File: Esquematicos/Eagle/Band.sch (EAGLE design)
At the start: 11 parts

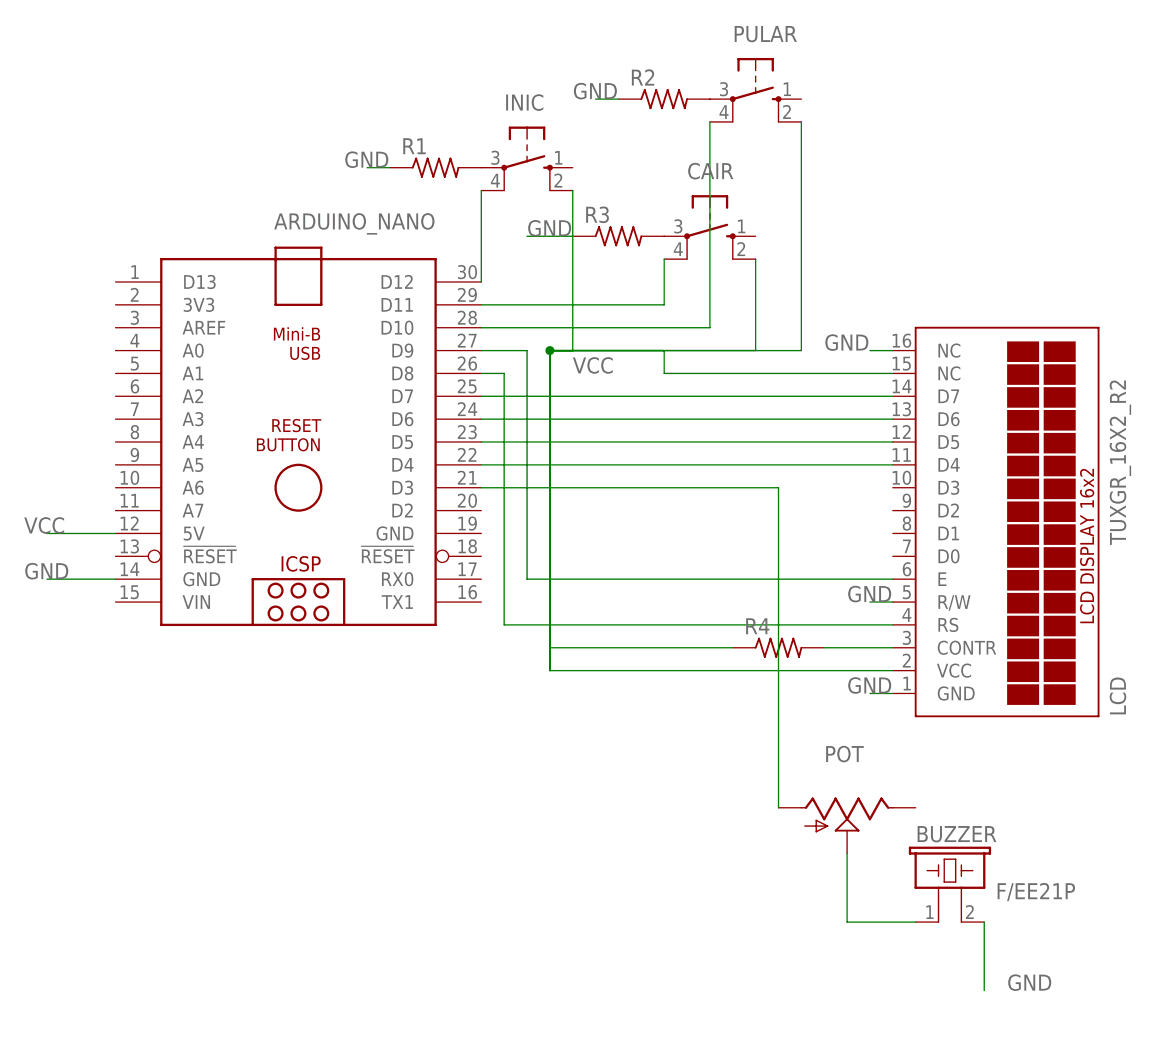
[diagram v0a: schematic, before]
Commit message: Editando Esquemático Eagle Band
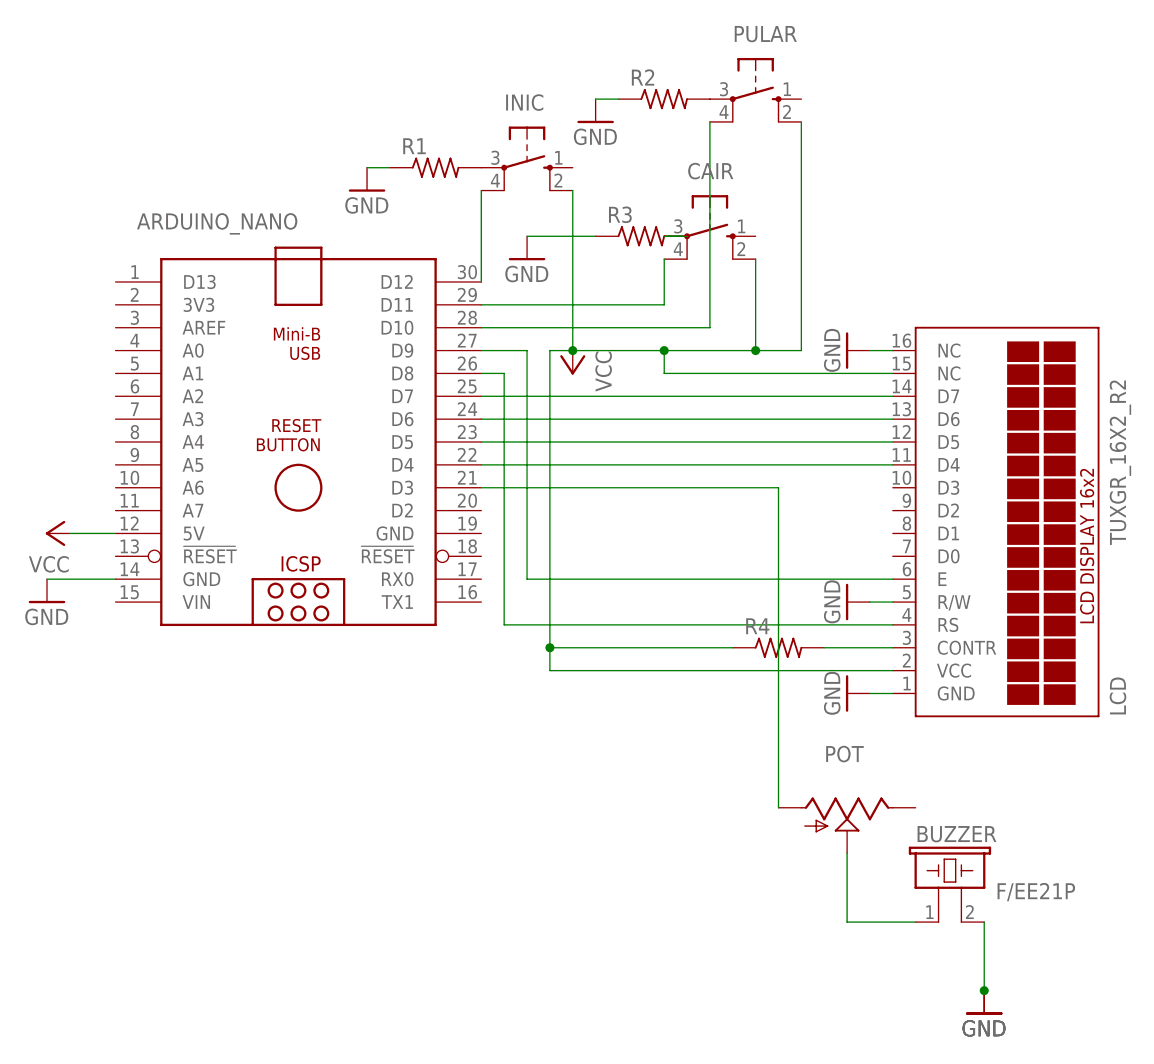
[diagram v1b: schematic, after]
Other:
- moved on the sheet: R3

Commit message: PCB da Band add
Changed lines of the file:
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@@
 <?xml version="1.0" encoding="utf-8"?>
 <!DOCTYPE eagle SYSTEM "eagle.dtd">
-<eagle version="9.6.1">
+<eagle version="9.1.0">
 <drawing>
 <settings>
-<setting alwaysvectorfont="no"/>
+<setting alwaysvectorfont="yes"/>
 <setting verticaltext="up"/>
 </settings>
@@
 <part name="GND7" library="supply1" library_urn="urn:adsk.eagle:library:371" deviceset="GND" device=""/>
 <part name="GND8" library="supply1" library_urn="urn:adsk.eagle:library:371" deviceset="GND" device=""/>
-<part name="GND9" library="supply1" library_urn="urn:adsk.eagle:library:371" deviceset="GND" device=""/>
 <part name="GND10" library="supply1" library_urn="urn:adsk.eagle:library:371" deviceset="GND" device=""/>
 <part name="P+1" library="supply1" library_urn="urn:adsk.eagle:library:371" deviceset="VCC" device=""/>
@@
 <attribute name="VALUE" x="114.3" y="144.78" size="1.778" layer="96"/>
 </instance>
-<instance part="GND9" gate="1" x="160.02" y="48.26" smashed="yes">
-<attribute name="VALUE" x="157.48" y="45.72" size="1.778" layer="96"/>
-</instance>
-<instance part="GND10" gate="1" x="160.02" y="48.26" smashed="yes">
-<attribute name="VALUE" x="157.48" y="45.72" size="1.778" layer="96"/>
+<instance part="GND10" gate="1" x="160.02" y="50.8" smashed="yes">
+<attribute name="VALUE" x="157.48" y="48.26" size="1.778" layer="96"/>
 </instance>
 <instance part="P+1" gate="VCC" x="55.88" y="101.6" smashed="yes" rot="R90">
@@
 <segment>
 <pinref part="BUZZER" gate="G$1" pin="2"/>
-<wire x1="160.02" y1="58.42" x2="160.02" y2="50.8" width="0.1524" layer="91"/>
-<pinref part="GND9" gate="1" pin="GND"/>
+<wire x1="160.02" y1="58.42" x2="160.02" y2="53.34" width="0.1524" layer="91"/>
 <pinref part="GND10" gate="1" pin="GND"/>
-<junction x="160.02" y="50.8"/>
-</segment>
-<segment>
+</segment>
+<segment>

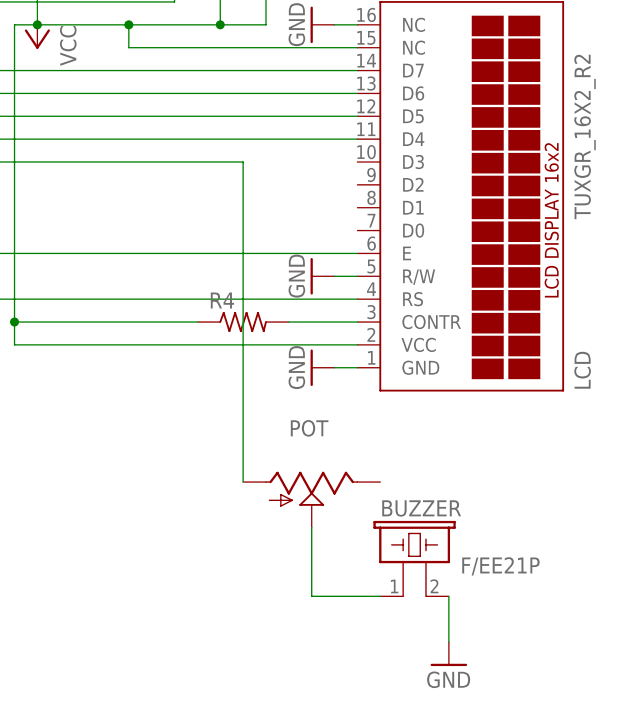
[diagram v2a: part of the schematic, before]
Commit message: Esquemático atualizado com os componentes 3D
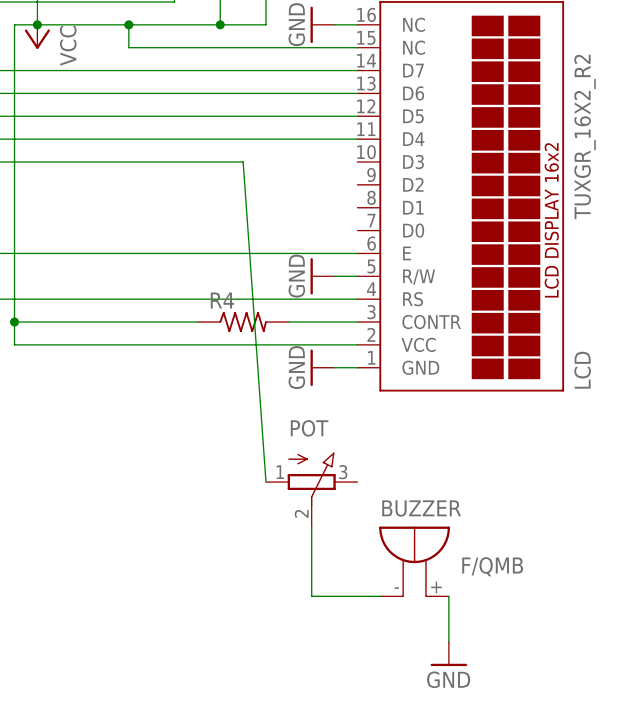
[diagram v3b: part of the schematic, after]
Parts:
- BUZZER: value F/EE21P -> F/QMB; device buzzer:F/EE21P -> buzzer:F/QMB
- CAIR, INIC, PULAR: device switch-omron:10-XX -> switch-omron:40-XX
- POT: device pot:TRIM_US-CIP20C-6MM -> pot:3RP/1610N
- R1, R2, R3, R4: device rcl:R-US_0204/7 -> resistor:R-US_0207/10
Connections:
- net GND: now also BUZZER.-; no longer BUZZER.2
- net N$15: now also BUZZER.+; no longer BUZZER.1
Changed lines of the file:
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@@
 <?xml version="1.0" encoding="utf-8"?>
 <!DOCTYPE eagle SYSTEM "eagle.dtd">
-<eagle version="9.1.0">
+<eagle version="9.6.2">
 <drawing>
 <settings>
@@
 <layers>
 <layer number="1" name="Top" color="4" fill="1" visible="no" active="no"/>
+<layer number="2" name="Route2" color="1" fill="3" visible="no" active="no"/>
+<layer number="3" name="Route3" color="4" fill="3" visible="no" active="no"/>
+<layer number="4" name="Route4" color="1" fill="4" visible="no" active="no"/>
+<layer number="5" name="Route5" color="4" fill="4" visible="no" active="no"/>
+<layer number="6" name="Route6" color="1" fill="8" visible="no" active="no"/>
+<layer number="7" name="Route7" color="4" fill="8" visible="no" active="no"/>
+<layer number="8" name="Route8" color="1" fill="2" visible="no" active="no"/>
+<layer number="9" name="Route9" color="4" fill="2" visible="no" active="no"/>
+<layer number="10" name="Route10" color="1" fill="7" visible="no" active="no"/>
+<layer number="11" name="Route11" color="4" fill="7" visible="no" active="no"/>
+<layer number="12" name="Route12" color="1" fill="5" visible="no" active="no"/>
+<layer number="13" name="Route13" color="4" fill="5" visible="no" active="no"/>
+<layer number="14" name="Route14" color="1" fill="6" visible="no" active="no"/>
+<layer number="15" name="Route15" color="4" fill="6" visible="no" active="no"/>
 <layer number="16" name="Bottom" color="1" fill="1" visible="no" active="no"/>
 <layer number="17" name="Pads" color="2" fill="1" visible="no" active="no"/>
@@
 <layer number="97" name="Info" color="7" fill="1" visible="yes" active="yes"/>
 <layer number="98" name="Guide" color="6" fill="1" visible="yes" active="yes"/>
+<layer number="99" name="SpiceOrder" color="5" fill="1" visible="yes" active="yes"/>
 </layers>
 <schematic xreflabel="%F%N/%S.%C%R" xrefpart="/%S.%C%R">
@@
 <parts>
 <part name="FRAME1" library="frames" library_urn="urn:adsk.eagle:library:229" deviceset="A4P-LOC" device=""/>
-<part name="PULAR" library="switch-omron" library_urn="urn:adsk.eagle:library:377" deviceset="10-XX" device="" package3d_urn="urn:adsk.eagle:package:27496/1"/>
-<part name="CAIR" library="switch-omron" library_urn="urn:adsk.eagle:library:377" deviceset="10-XX" device="" package3d_urn="urn:adsk.eagle:package:27496/1"/>
-<part name="INIC" library="switch-omron" library_urn="urn:adsk.eagle:library:377" deviceset="10-XX" device="" package3d_urn="urn:adsk.eagle:package:27496/1"/>
-<part name="ARDUINO_NANO" library="ArduinoNanoV30" deviceset="ARDUINO_NANO" device=""/>
-<part name="LCD" library="display-lcd" library_urn="urn:adsk.eagle:library:214" deviceset="TUXGR_16X2_R2" device="" package3d_urn="urn:adsk.eagle:package:13139/1"/>
-<part name="R1" library="rcl" library_urn="urn:adsk.eagle:library:334" deviceset="R-US_" device="0204/7" package3d_urn="urn:adsk.eagle:package:23498/1"/>
-<part name="R2" library="rcl" library_urn="urn:adsk.eagle:library:334" deviceset="R-US_" device="0204/7" package3d_urn="urn:adsk.eagle:package:23498/1"/>
-<part name="R3" library="rcl" library_urn="urn:adsk.eagle:library:334" deviceset="R-US_" device="0204/7" package3d_urn="urn:adsk.eagle:package:23498/1"/>
-<part name="R4" library="rcl" library_urn="urn:adsk.eagle:library:334" deviceset="R-US_" device="0204/7" package3d_urn="urn:adsk.eagle:package:23498/1"/>
-<part name="BUZZER" library="buzzer" library_urn="urn:adsk.eagle:library:113" deviceset="F/EE21P" device="" package3d_urn="urn:adsk.eagle:package:5263/1"/>
-<part name="POT" library="pot" library_urn="urn:adsk.eagle:library:331" deviceset="TRIM_US-" device="CIP20C-6MM" package3d_urn="urn:adsk.eagle:package:22723/1"/>
+<part name="PULAR" library="switch-omron" library_urn="urn:adsk.eagle:library:377" deviceset="40-XX" device="" package3d_urn="urn:adsk.eagle:package:27483/1" override_package3d_urn="urn:adsk.eagle:package:22090944/2" override_package_urn="urn:adsk.eagle:footprint:27470/1"/>
+<part name="CAIR" library="switch-omron" library_urn="urn:adsk.eagle:library:377" deviceset="40-XX" device="" package3d_urn="urn:adsk.eagle:package:27483/1" override_package3d_urn="urn:adsk.eagle:package:22090917/2" override_package_urn="urn:adsk.eagle:footprint:27470/1"/>
+<part name="INIC" library="switch-omron" library_urn="urn:adsk.eagle:library:377" deviceset="40-XX" device="" package3d_urn="urn:adsk.eagle:package:27483/1" override_package3d_urn="urn:adsk.eagle:package:22090920/2" override_package_urn="urn:adsk.eagle:footprint:27470/1"/>
+<part name="ARDUINO_NANO" library="ArduinoNanoV30" deviceset="ARDUINO_NANO" device="" override_package3d_urn="urn:adsk.eagle:package:22090949/2" override_package_urn="urn:adsk.eagle:footprint:22090950/1"/>
+<part name="LCD" library="display-lcd" library_urn="urn:adsk.eagle:library:214" deviceset="TUXGR_16X2_R2" device="" package3d_urn="urn:adsk.eagle:package:13139/1" override_package3d_urn="urn:adsk.eagle:package:22090958/2" override_package_urn="urn:adsk.eagle:footprint:13120/1"/>
+<part name="R1" library="resistor" library_urn="urn:adsk.eagle:library:348" deviceset="R-US_" device="0207/10" package3d_urn="urn:adsk.eagle:package:25939/1" override_package3d_urn="urn:adsk.eagle:package:22090895/2" override_package_urn="urn:adsk.eagle:footprint:25501/1"/>
+<part name="R2" library="resistor" library_urn="urn:adsk.eagle:library:348" deviceset="R-US_" device="0207/10" package3d_urn="urn:adsk.eagle:package:25939/1" override_package3d_urn="urn:adsk.eagle:package:22090907/2" override_package_urn="urn:adsk.eagle:footprint:25501/1"/>
+<part name="R3" library="resistor" library_urn="urn:adsk.eagle:library:348" deviceset="R-US_" device="0207/10" package3d_urn="urn:adsk.eagle:package:25939/1" override_package3d_urn="urn:adsk.eagle:package:22090897/2" override_package_urn="urn:adsk.eagle:footprint:25501/1"/>
+<part name="R4" library="resistor" library_urn="urn:adsk.eagle:library:348" deviceset="R-US_" device="0207/10" package3d_urn="urn:adsk.eagle:package:25939/1" override_package3d_urn="urn:adsk.eagle:package:22090889/2" override_package_urn="urn:adsk.eagle:footprint:25501/1"/>
+<part name="BUZZER" library="buzzer" library_urn="urn:adsk.eagle:library:113" deviceset="F/QMB" device="" package3d_urn="urn:adsk.eagle:package:5270/1" override_package3d_urn="urn:adsk.eagle:package:22090835/2" override_package_urn="urn:adsk.eagle:footprint:5226/1"/>
+<part name="POT" library="pot" library_urn="urn:adsk.eagle:library:331" deviceset="3RP/1610N" device="" package3d_urn="urn:adsk.eagle:package:22726/1" override_package3d_urn="urn:adsk.eagle:package:22090822/2" override_package_urn="urn:adsk.eagle:footprint:22673/1"/>
 <part name="GND1" library="supply1" library_urn="urn:adsk.eagle:library:371" deviceset="GND" device=""/>
 <part name="GND3" library="supply1" library_urn="urn:adsk.eagle:library:371" deviceset="GND" device=""/>
@@
 </segment>
 <segment>
-<pinref part="BUZZER" gate="G$1" pin="2"/>
+<pinref part="BUZZER" gate="G$1" pin="-"/>
 <wire x1="160.02" y1="58.42" x2="160.02" y2="53.34" width="0.1524" layer="91"/>
 <pinref part="GND10" gate="1" pin="GND"/>
@@
 <pinref part="POT" gate="G$1" pin="A"/>
 <wire x1="104.14" y1="106.68" x2="137.16" y2="106.68" width="0.1524" layer="91"/>
-<wire x1="137.16" y1="106.68" x2="137.16" y2="71.12" width="0.1524" layer="91"/>
+<wire x1="137.16" y1="106.68" x2="139.7" y2="71.12" width="0.1524" layer="91"/>
 </segment>
 </net>
@@
 <pinref part="POT" gate="G$1" pin="S"/>
 <wire x1="144.78" y1="66.04" x2="144.78" y2="58.42" width="0.1524" layer="91"/>
-<pinref part="BUZZER" gate="G$1" pin="1"/>
+<pinref part="BUZZER" gate="G$1" pin="+"/>
 <wire x1="144.78" y1="58.42" x2="152.4" y2="58.42" width="0.1524" layer="91"/>
 </segment>
@@
 packages will not be understood (or retained) with this version.
 </note>
-<note version="8.4" severity="warning">
-Since Version 8.4, EAGLE supports properties for SPICE simulation.
-Probes in schematics and SPICE mapping objects found in parts and library devices
-will not be understood with this version. Update EAGLE to the latest version
-for full support of SPICE simulation.
+<note version="9.4" severity="warning">
+Since Version 9.4, EAGLE supports the overriding of 3D packages
+in schematics and board files. Those overridden 3d packages
+will not be understood (or retained) with this version.
 </note>
 </compatibility>
